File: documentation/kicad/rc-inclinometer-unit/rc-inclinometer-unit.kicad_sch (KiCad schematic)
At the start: 8 parts

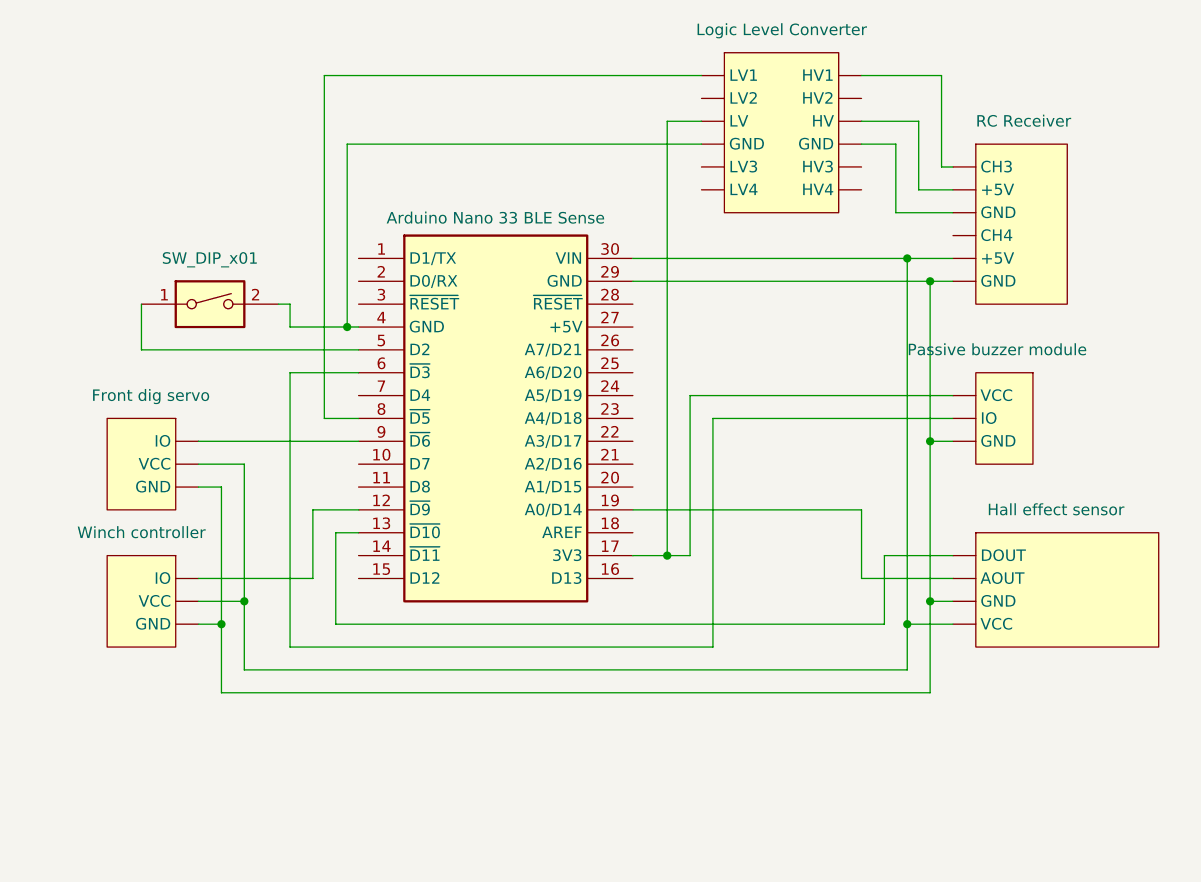
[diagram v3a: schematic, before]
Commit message: new winch controller schema
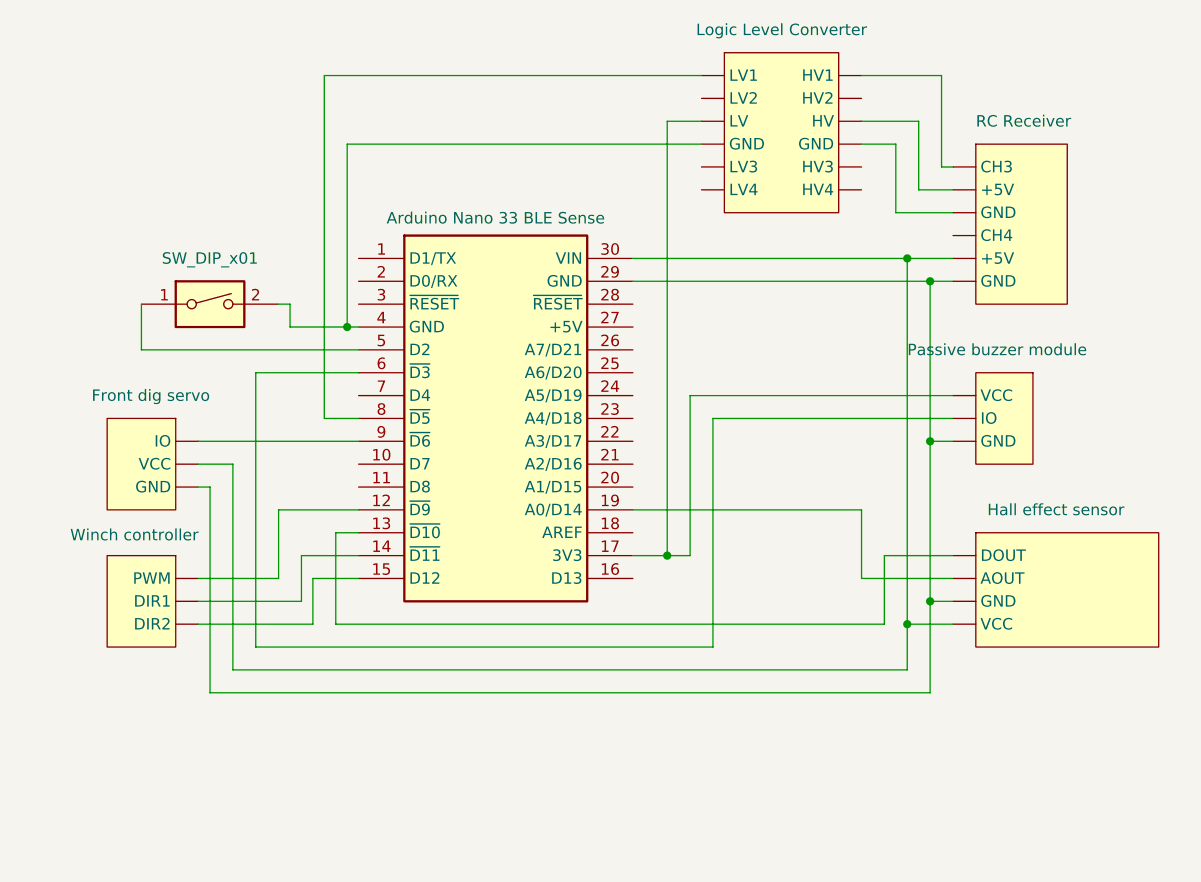
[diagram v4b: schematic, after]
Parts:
- removed U?: Winch controller, symbol rc-inclinometer-unit-custom-library:Winch controller
- added U1: Winch controller, symbol rc-inclinometer-unit-custom-library:Winch controller L298N
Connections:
- net at U?.12 (~{D9}): now also U1. (PWM)
- net at U?.14 (~{D11}): now also U1. (PWM)
- net at U?.15 (D12): now also U1. (PWM)
- net at U?. (LV4): now also U?. (GND)
- net at U?. (GND): no longer U?. (LV4)
- new net: U?. (LV4), U?. (VCC), U?.17 (3V3)
- new net: U?. (GND), U?. (VCC), U?. (VCC), U?. (VCC), U?.29 (GND)
- new net: U?. (GND), U?. (LV4) (x2)
- now unconnected: U?. (GND), U?. (GND), U?. (GND)

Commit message: update to Kicad 9.0
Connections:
- net at U?. (HV4): now also U?. (GND)
- net at U?. (GND): no longer U?. (LV4)
- new net: U?. (GND), U?. (HV4), U?.17 (3V3)
- new net: U?. (GND), U?. (GND), U?. (GND), U?. (VCC), U?.29 (GND)
- new net: U?. (GND), U?. (HV4) (x2)
- now unconnected: U?. (GND), U?. (GND), U?. (GND)
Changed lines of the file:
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@@
 (kicad_sch
-	(version 20231120)
+	(version 20250114)
 	(generator "eeschema")
-	(generator_version "8.0")
+	(generator_version "9.0")
 	(paper "A4")
 	(junction
@@
 		)
 	)
+	(embedded_fonts no)
 )

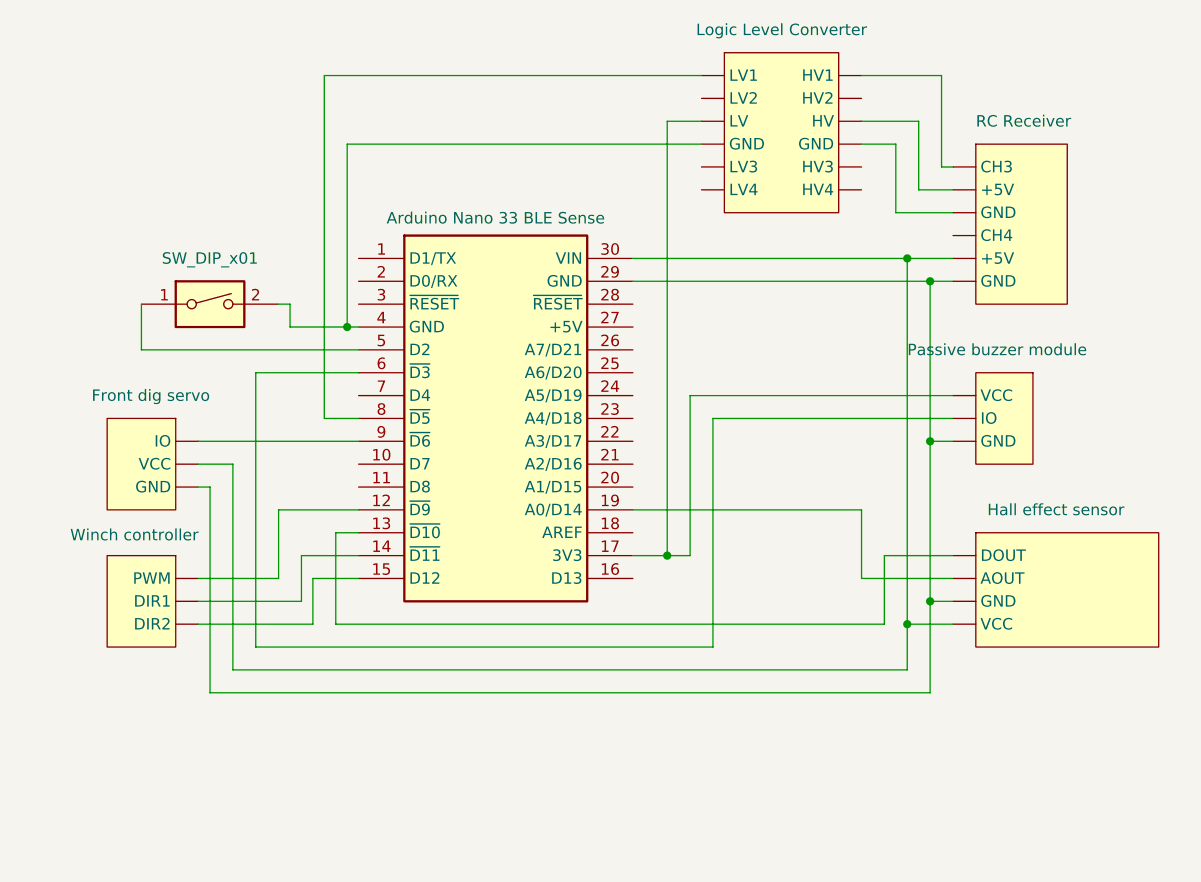
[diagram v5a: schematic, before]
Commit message: changed pins for speed sensor and winch control
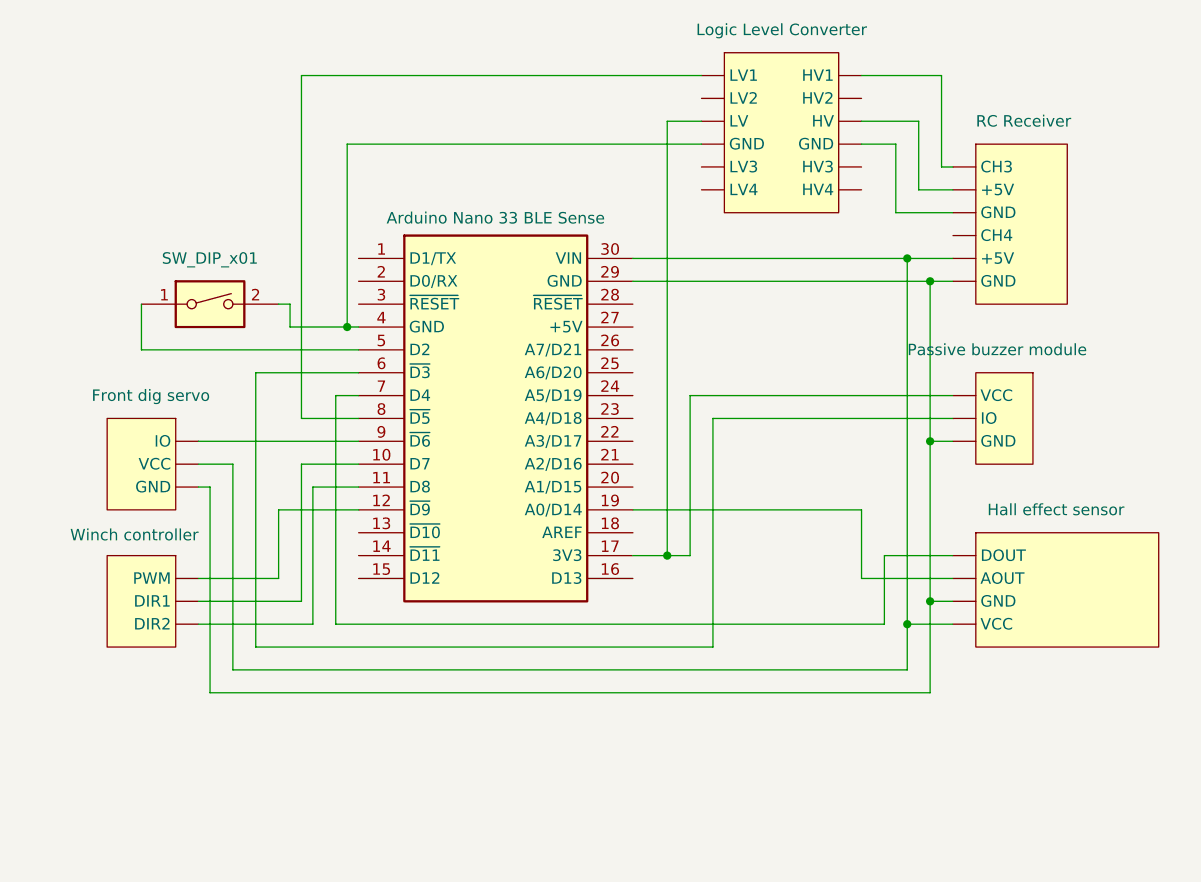
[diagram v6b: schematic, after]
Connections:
- net at U?.10 (D7): now also U1. (DIR2)
- net at U?.11 (D8): now also U1. (DIR2)
- net at U?.13 (~{D10}): no longer U?. (VCC)
- net at U?.14 (~{D11}): no longer U1. (DIR2)
- net at U?.15 (D12): no longer U1. (DIR2)
- net at U?.7 (D4): now also U?. (VCC)
- net at U?. (HV4): now also U?. (GND)
- net at U?. (GND): no longer U?. (HV4)
- new net: U?. (GND), U?. (HV4), U?.17 (3V3)
- new net: U?. (GND), U?. (GND), U?. (GND), U?. (VCC), U?.29 (GND)
- new net: U?. (GND), U?. (GND), U?. (VCC), U?.30 (VIN)
- new net: U?. (GND), U?. (HV4) (x2)
- now unconnected: U?. (GND), U?. (GND), U?. (GND), U?. (GND)
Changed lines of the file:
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@@
+	(wire
+		(pts
+			(xy 120.65 109.22) (xy 120.65 93.98)
+		)
+		(stroke
+			(width 0)
+			(type default)
+		)
+	)
 	(wire
 		(pts
@@
 	(wire
 		(pts
-			(xy 124.46 101.6) (xy 124.46 111.76)
+			(xy 124.46 86.36) (xy 124.46 111.76)
 		)
 		(stroke
@@
 	(wire
 		(pts
-			(xy 123.19 50.8) (xy 165.1 50.8)
+			(xy 120.65 50.8) (xy 165.1 50.8)
 		)
 		(stroke
@@
 	(wire
 		(pts
-			(xy 123.19 88.9) (xy 123.19 50.8)
+			(xy 120.65 88.9) (xy 120.65 50.8)
 		)
 		(stroke
@@
 	(wire
 		(pts
-			(xy 127 101.6) (xy 124.46 101.6)
-		)
-		(stroke
-			(width 0)
-			(type default)
-		)
-	)
-	(wire
-		(pts
 			(xy 109.22 93.98) (xy 113.03 93.98)
 		)
@@
 	(wire
 		(pts
+			(xy 121.92 111.76) (xy 121.92 96.52)
+		)
+		(stroke
+			(width 0)
+			(type default)
+		)
+	)
+	(wire
+		(pts
 			(xy 190.5 109.22) (xy 190.5 119.38)
 		)
@@
 	(wire
 		(pts
-			(xy 121.92 106.68) (xy 121.92 111.76)
-		)
-		(stroke
-			(width 0)
-			(type default)
-		)
-	)
-	(wire
-		(pts
 			(xy 118.11 99.06) (xy 118.11 106.68)
 		)
@@
 	(wire
 		(pts
+			(xy 121.92 96.52) (xy 127 96.52)
+		)
+		(stroke
+			(width 0)
+			(type default)
+		)
+	)
+	(wire
+		(pts
 			(xy 185.42 104.14) (xy 193.04 104.14)
 		)
@@
 	(wire
 		(pts
+			(xy 124.46 86.36) (xy 127 86.36)
+		)
+		(stroke
+			(width 0)
+			(type default)
+		)
+	)
+	(wire
+		(pts
 			(xy 186.69 66.04) (xy 186.69 58.42)
 		)
@@
 	(wire
 		(pts
-			(xy 123.19 88.9) (xy 127 88.9)
-		)
-		(stroke
-			(width 0)
-			(type default)
-		)
-	)
-	(wire
-		(pts
-			(xy 127 104.14) (xy 120.65 104.14)
+			(xy 120.65 93.98) (xy 127 93.98)
+		)
+		(stroke
+			(width 0)
+			(type default)
+		)
+	)
+	(wire
+		(pts
+			(xy 120.65 88.9) (xy 127 88.9)
 		)
 		(stroke
@@
 	(wire
 		(pts
-			(xy 127 106.68) (xy 121.92 106.68)
-		)
-		(stroke
-			(width 0)
-			(type default)
-		)
-	)
-	(wire
-		(pts
 			(xy 182.88 58.42) (xy 186.69 58.42)
 		)
 		(stroke
-			(width 0)
-			(type default)
-		)
-	)
-	(wire
-		(pts
-			(xy 120.65 104.14) (xy 120.65 109.22)
-		)
-		(stroke

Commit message: use AT24C256 module to store preferences instead of internal EEPROM which stopped working
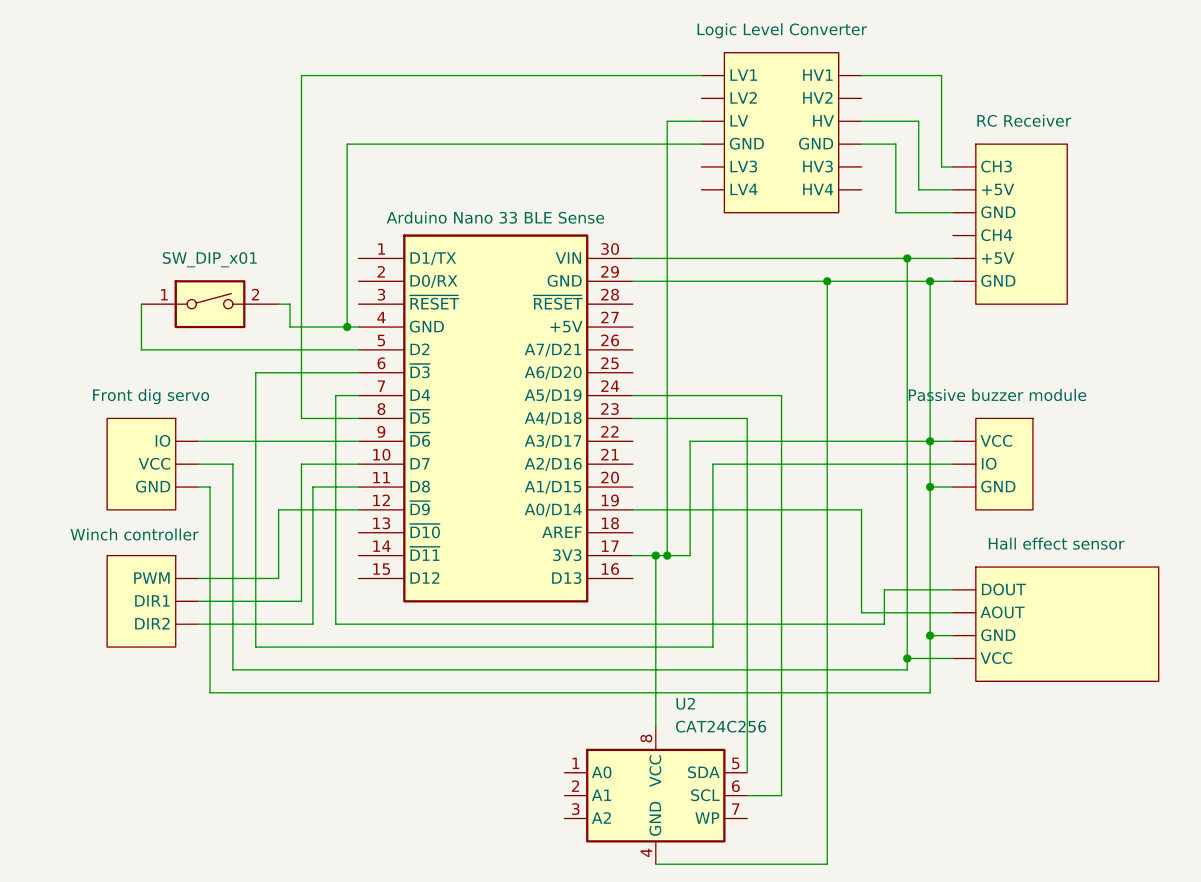
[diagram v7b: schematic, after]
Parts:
- added U2: CAT24C256, symbol Memory_EEPROM:CAT24C256
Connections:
- net at U?.23 (A4/D18): now also U2.5 (SDA)
- net at U?.24 (A5/D19): now also U2.6 (SCL)
- net at U?. (HV4): now also U?. (GND)
- net at U?. (GND): no longer U?. (HV4)
- new net: U2.4 (GND), U2.8 (VCC), U?. (GND), U?. (GND), U?. (GND), U?. (HV4), U?. (VCC), U?.17 (3V3), U?.29 (GND)
- new net: U?. (GND), U?. (GND), U?. (VCC), U?.30 (VIN)
- new net: U?. (GND), U?. (HV4) (x2)
- now unconnected: U?. (GND), U?. (GND), U?. (GND), U?. (GND)
